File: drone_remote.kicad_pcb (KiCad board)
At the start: 2 copper layers, 7 x 9.2 mm, 99 parts, among them J1 USBC, J10 HEADER_C, J2 BAT, J3 UART, J4 SWI, J5 OLDED_SMALL, J6 OLED_BIG, J7 RFM_SOCKET, J8 RFM_SOCKET, J9 HEADER_AB, Q1 PMOS, SW1 RST_BTN, SW2 PUSH_BTN_U, SW3 PUSH_BTN_L, SW4 PUSH_BTN_R, SW5 PUSH_BTN_D, SW6 ENC1, SW7 ENC2, U1 STM32F411RETx, U2 TC1262-33, U3 SN74ALVC14PWR, U4 SN74ALVC14PWR, U5 INA180A2, U6 FT230XS, X1 32.768KHz, X2 8MHz

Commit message: update
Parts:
- removed C11: 12p, Capacitor_SMD:C_0402_1005Metric
- removed C12: 36p, Capacitor_SMD:C_0402_1005Metric
- removed C18: 100n, Capacitor_SMD:C_0805_2012Metric
- removed D7: UART_TX, LED_SMD:LED_0201_0603Metric
- removed D8: HEARTBEAT, Inductor_SMD:L_0201_0603Metric
- removed J10: HEADER_C, Connector_PinSocket_1.27mm:PinSocket_2x16_P1.27mm_Vertical
- removed J9: HEADER_AB, Connector_PinSocket_1.27mm:PinSocket_2x16_P1.27mm_Vertical
- removed JP2: BLK_OFF, Connector_PinSocket_1.27mm:PinSocket_1x02_P1.27mm_Vertical
- removed JP3: BLK_ON, Connector_PinSocket_1.27mm:PinSocket_1x02_P1.27mm_Vertical
- removed R14, R15: 660, Resistor_SMD:R_0805_2012Metric
- removed R9: 0.1, Resistor_SMD:R_0805_2012Metric
- removed U5: INA180A2, Package_TO_SOT_SMD:SOT-23-5
- removed X2: 8MHz, CRYSTAL_ECS-80-18-5PX-TR_ECS:CRYSTAL_ECS-80-18-5PX-TR_ECS
- added C33: 100n, Capacitor_SMD:C_0805_2012Metric, F.Cu at (164.2, 116.8)
- added H1: MountingHole, MountingHole:MountingHole_2.2mm_M2, F.Cu at (114.0, 76.5)
- added H2: MountingHole, MountingHole:MountingHole_2.2mm_M2, F.Cu at (114.0, 149.1)
- added H3: MountingHole, MountingHole:MountingHole_2.2mm_M2, F.Cu at (258.5, 76.5)
- added H4: MountingHole, MountingHole:MountingHole_2.2mm_M2, F.Cu at (258.5, 149.0)
- added JP1: Jumper_2_Bridged, Connector_PinHeader_2.54mm:PinHeader_1x02_P2.54mm_Vertical, F.Cu at (120.6, 81.8)
- added JP4: Jumper_2_Bridged, Connector_PinHeader_2.54mm:PinHeader_1x02_P2.54mm_Vertical, F.Cu at (147.0, 115.6)
- C10: value 12p -> 1u
- C13: value 36p -> 10p
- C14: value 100n -> 10p; footprint Capacitor_SMD:C_0805_2012Metric -> Capacitor_SMD:C_0402_1005Metric
- C15: value 1u -> 100n
- C17: value 0.1u -> 1u
- C19: value 47p -> 100n; footprint Capacitor_SMD:C_0201_0603Metric -> Capacitor_SMD:C_0805_2012Metric
- C2, C3, C4, C5, C6, C7, C8, C9: footprint Capacitor_SMD:C_0805_2012Metric -> Capacitor_SMD:C_0402_1005Metric
- C21: value 100n -> 47p; footprint Capacitor_SMD:C_0805_2012Metric -> Capacitor_SMD:C_0201_0603Metric
- D1, D2, D3: footprint Diode_SMD:D_0201_0603Metric -> Diode_SMD:D_0402_1005Metric
- D6: value UART_RX -> HEARTBEAT; footprint LED_SMD:LED_0201_0603Metric -> Inductor_SMD:L_0201_0603Metric
- J1: footprint SAMESKY_UJ20-C-H-G-MSMT-3-P16-TR:SAMESKY_UJ20-C-H-G-MSMT-3-P16-TR -> drone_remote:GCT_USB4105-GF-A
- J2: value BAT -> Conn_01x02_Socket; footprint Connector_PinSocket_2.54mm:PinSocket_1x02_P2.54mm_Vertical -> Connector_PinHeader_2.54mm:PinHeader_1x02_P2.54mm_Vertical
- J4: value SWI -> Conn_01x05_Pin; footprint Connector_PinSocket_1.00mm:PinSocket_1x05_P1.00mm_Vertical -> Connector_PinHeader_2.54mm:PinHeader_1x05_P2.54mm_Vertical
- J5: value OLDED_SMALL -> Conn_01x04_Socket; footprint Connector_PinSocket_1.00mm:PinSocket_1x04_P1.00mm_Vertical -> Connector_PinSocket_2.54mm:PinSocket_1x04_P2.54mm_Vertical
- J6: value OLED_BIG -> Conn_01x08_Socket; footprint Connector_PinSocket_1.00mm:PinSocket_1x08_P1.00mm_Vertical -> Connector_PinSocket_2.54mm:PinSocket_1x08_P2.54mm_Vertical
- J7, J8: value RFM_SOCKET -> Conn_01x09_Socket; footprint Connector_PinSocket_1.00mm:PinSocket_1x09_P1.00mm_Vertical -> Connector_PinSocket_2.54mm:PinSocket_1x09_P2.54mm_Vertical
- L1: value L_VDDA -> 120R; footprint Inductor_SMD:L_0805_2012Metric -> Inductor_SMD:L_0603_1608Metric
- L2: value L_UART -> 120R; footprint Inductor_SMD:L_0805_2012Metric -> Inductor_SMD:L_0603_1608Metric
- R1: value 47k -> 10k
- R2: value 2k -> 660
- R5: value 660 -> 10k
- SW2: value PUSH_BTN_U -> RST_BTN
- SW3: value PUSH_BTN_L -> RST_BTN
- SW4: value PUSH_BTN_R -> RST_BTN
- SW5: value PUSH_BTN_D -> RST_BTN
- X1: value 32.768KHz -> 8MHZ; footprint XTAL_7X-TR_ECS:XTAL_7X-TR_ECS -> ECS-80-10:SMD_ECS-80-10-3M-TR_ECS
- moved J3 185.2 mm to (212.3, 81.2), turned to 180 degrees
- moved C14 182.4 mm to (186.5, 120.4), turned to 180 degrees
- moved L2 179.7 mm to (215.7, 90.2), turned to -90 degrees
- moved C19 179.5 mm to (216.7, 87.3), turned to 180 degrees
- moved C20 175.5 mm to (211.9, 84.8), turned to 0 degrees
- moved J1 174.4 mm to (186.2, 75.9), turned to 180 degrees
- moved R13 170.6 mm to (212.1, 88.7), turned to 90 degrees
- moved R12 168.7 mm to (209.8, 88.7), turned to -90 degrees
- moved D1 167.1 mm to (187.3, 82.8), turned to 0 degrees
- moved D2 165.6 mm to (185.1, 82.8), turned to 180 degrees
- moved J2 164.7 mm to (173.5, 77.1), turned to -90 degrees
- moved R7 162.6 mm to (193.9, 78.0), turned to 0 degrees
- moved C21 161.2 mm to (210.2, 84.8), turned to 180 degrees
- moved D3 153.9 mm to (176.6, 82.0)
- moved U6 153.6 mm to (210.8, 94.7), turned to 180 degrees
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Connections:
- net Net-(D4-A) renamed /V_USB
- net Net-(D5-A) renamed /V_BAT
- net Net-(J2-Pin_2) renamed +5V
- net Net-(U6-USBDM) renamed /USBD-
- net Net-(U6-USBDP) renamed /USBD+
- net RFM_nRST renamed /RFM_nRST
- net SPI1_MISO renamed /SPI1_MISO
- net SPI1_MOSI renamed /SPI1_MOSI
- net SPI1_SCK renamed /SPI1_SCK
- net SPI1_nCS renamed /SPI1_nCS
- net SWCLK renamed /SWCLK
- C10 pad 1: GND -> +3.3V
- C10 pad 2: Net-(U1-PC15) -> GND
- C13 pad 2: Net-(U1-PH1) -> /OSC_OUT
- C14 pad 2: Net-(D3-A1) -> /OSC_IN
- C15 pad 1: Net-(D4-K) -> GND
- C15 pad 2: GND -> VBUS
- C16 pad 1: 3.3V -> /REG_IN
- C17 pad 1: 3.3V -> +3.3V
- C19 pad 1: Net-(J3-D-) -> GND
- C19 pad 2: GND -> Net-(J3-VBUS)
- C2 pad 1: 3.3V -> GND
- C2 pad 2: GND -> +3.3V
- C20 pad 1: Net-(J3-D+) -> /D-
- C21 pad 1: Net-(U6-3V3OUT) -> /D+
- C22 pad 1: GND -> Net-(U6-3V3OUT)
- C22 pad 2: Net-(U3-1A) -> GND
- C23 pad 2: Net-(U3-2A) -> /SW2
- C24 pad 1: Net-(U3-4A) -> GND
- C24 pad 2: GND -> /SW3
- C25 pad 2: Net-(U3-3A) -> /SW4
- C26 pad 1: GND -> /SW5
- C26 pad 2: Net-(U4-1A) -> GND
- C27 pad 1: Net-(U4-2A) -> GND
- C27 pad 2: GND -> /ENC1_A
- C28 pad 1: Net-(U4-3A) -> /ENC1_C
- C29 pad 1: GND -> /ENC1_SW
- C29 pad 2: Net-(U4-6A) -> GND
- C3 pad 2: 3.3V -> +3.3V
- C30 pad 2: Net-(U4-5A) -> /ENC2_A
- C31 pad 2: Net-(U4-4A) -> /ENC2_C
- C32 pad 2: nRST -> /ENC2_SW
- C4 pad 2: 3.3V -> +3.3V
- C5 pad 2: 3.3V -> +3.3V
- C6 pad 2: 3.3V -> +3.3V
- C7 pad 2: 3.3V -> +3.3V
- C8 pad 2: 3.3V -> +3.3VA
- C9 pad 1: GND -> +3.3VA
- C9 pad 2: 3.3V -> GND
- D1 pad 1: USB_OTG_FS_DM -> /USB_OTG_FS-
- D2 pad 1: USB_OTG_FS_DP -> /USB_OTG_FS+
- D3 pad 1: Net-(D3-A1) -> VBUS
- D4 pad 1: Net-(D4-K) -> /REG_IN
- D5 pad 1: Net-(D4-K) -> /REG_IN
- D6 pad 1: Net-(D6-K) -> GND
- F1 pad 1: Net-(D3-A1) -> VBUS
- J1 pad A4_B9: Net-(D3-A1) -> VBUS
- J1 pad A6: USB_OTG_FS_DP -> unconnected-(J1-DP1-PadA6)
- J1 pad A7: USB_OTG_FS_DM -> unconnected-(J1-DN1-PadA7)
- J1 pad B6: unconnected-(J1-DP2-PadB6) -> /USB_OTG_FS+
- J1 pad B7: unconnected-(J1-DN2-PadB7) -> /USB_OTG_FS-
- J3 pad 2: Net-(J3-D-) -> /D-
- J3 pad 3: Net-(J3-D+) -> /D+
- J3 pad 6: GND -> unconnected-(J3-Shield-Pad6)
- J4 pad 1: GND -> +3.3V
- J4 pad 2: nRST -> /SWDIO
- J4 pad 4: SWDIO -> /nRST
- J4 pad 5: 3.3V -> GND
- J5 pad 1: 3.3V -> /I2C1_SDA
- J5 pad 2: GND -> /I2C1_SCL
- J5 pad 3: I2C1_SCL -> GND
- J5 pad 4: I2C1_SDA -> +3.3V
- J6 pad 2: 3.3V -> +3.3V
- J6 pad 3: SPI2_SCK -> /SPI3_SCK
- J6 pad 4: SPI2_MOSI -> /SPI3_MOSI
- J6 pad 5: ST7735_nRESET -> /ST7735_nRST
- J6 pad 6: ST7735_DC -> /ST7735_DC
- J6 pad 7: SPI2_NSS -> /SPI3_nCS
- J7 pad 1: 3.3V -> +3.3V
- J7 pad 3: RFM_EN -> /RFM_EN
- J7 pad 9: RFM__G0 -> /RFM_G0
- L1 pad 1: 3.3V -> +3.3VA
- L1 pad 2: Net-(U1-VDDA) -> +3.3V
- R1 pad 1: Net-(U1-BOOT0) -> GND
- R1 pad 2: GND -> /BOOT0
- R10 pad 1: Net-(D4-K) -> /REG_IN
- R10 pad 2: ADC_VOLTAGE -> /ADC_VOLTAGE
- R11 pad 1: ADC_VOLTAGE -> /ADC_VOLTAGE
- R12 pad 1: Net-(J3-D+) -> /D+
- R13 pad 2: Net-(J3-D-) -> /D-
- R16 pad 1: Net-(U3-1A) -> /SW2
- R16 pad 2: 3.3V -> +3.3V
- R17 pad 1: Net-(U3-2A) -> /SW3
- R17 pad 2: 3.3V -> +3.3V
- R18 pad 1: 3.3V -> +3.3V
- R18 pad 2: Net-(U3-4A) -> /SW5
- R19 pad 1: Net-(U3-3A) -> /SW4
- R19 pad 2: 3.3V -> +3.3V
- R2 pad 1: 3.3V -> Net-(D6-A)
- R2 pad 2: Net-(U1-BOOT0) -> /HB_LED
- R20 pad 1: Net-(U4-1A) -> /ENC1_A
- R20 pad 2: 3.3V -> +3.3V
- R21 pad 1: 3.3V -> +3.3V
- R21 pad 2: Net-(U4-2A) -> /ENC1_C
- R22 pad 1: 3.3V -> +3.3V
- R22 pad 2: Net-(U4-3A) -> /ENC1_SW
- R23 pad 1: Net-(U4-6A) -> /ENC2_A
- R23 pad 2: 3.3V -> +3.3V
- R24 pad 1: Net-(U4-5A) -> /ENC2_C
- R24 pad 2: 3.3V -> +3.3V
- R25 pad 1: Net-(U4-4A) -> /ENC2_SW
- R25 pad 2: 3.3V -> +3.3V
- R26 pad 2: 3.3V -> +3.3V
- R3 pad 1: SWDIO -> /SWDIO
- R3 pad 2: 3.3V -> +3.3V
- R4 pad 2: 3.3V -> +3.3V
- R5 pad 1: Net-(D8-A) -> Net-(J6-Pin_8)
- R5 pad 2: PC13 -> GND
- R6 pad 2: PC10 -> /MCU_LED
- SW1 pad 1: nRST -> /nRST
- SW1 pad 3: nRST -> /nRST
- SW2 pad 2: GND -> /SW2
- SW2 pad 3: Net-(U3-1A) -> GND
- SW2 pad 4: Net-(U3-1A) -> /SW2
- SW3 pad 2: GND -> /SW3
- SW3 pad 3: Net-(U3-2A) -> GND
- SW3 pad 4: Net-(U3-2A) -> /SW3
- SW4 pad 2: GND -> /SW4
- SW4 pad 3: Net-(U3-3A) -> GND
- SW4 pad 4: Net-(U3-3A) -> /SW4
- SW5 pad 2: GND -> /SW5
- SW5 pad 3: Net-(U3-4A) -> GND
- SW5 pad 4: Net-(U3-4A) -> /SW5
- SW6 pad A: Net-(U4-2A) -> /ENC1_C
- SW6 pad B: Net-(U4-1A) -> /ENC1_A
- SW6 pad S1: Net-(U4-3A) -> /ENC1_SW
- SW7 pad A: Net-(U4-6A) -> /ENC2_C
- SW7 pad B: Net-(U4-5A) -> /ENC2_A
- SW7 pad C: unconnected-(SW7-PadC) -> GND
- SW7 pad S1: GND -> /ENC2_SW
- SW7 pad S2: Net-(U4-4A) -> GND
- U1 pad 1: 3.3V -> +3.3V
- U1 pad 10: RFM__G0 -> unconnected-(U1-PC2-Pad10)
- U1 pad 11: PUSH_BTN3 -> unconnected-(U1-PC3-Pad11)
- U1 pad 13: Net-(U1-VDDA) -> +3.3VA
- U1 pad 14: TIM2_CH1 -> /TIM2_CH1
- U1 pad 15: TIM2_CH2 -> /TIM2_CH2
- U1 pad 16: ST7735_DC -> /ENC2_BTN
- U1 pad 17: ST7735_nRESET -> /ENC1_BTN
- U1 pad 19: 3.3V -> +3.3V
- U1 pad 2: PC13 -> /PUSH_BTN2
- U1 pad 24: PUSH_BTN4 -> /RFM_EN
- U1 pad 26: RFM_EN -> /RFM_G0
- U1 pad 27: PUSH_BTN1 -> /ADC_VOLTAGE
- U1 pad 28: PUSH_BTN2 -> /MCU_LED
- U1 pad 29: SPI2_SCK -> /HB_LED
- U1 pad 3: Net-(U1-PC14) -> /PUSH_BTN3
- U1 pad 32: 3.3V -> +3.3V
- U1 pad 33: SPI2_NSS -> unconnected-(U1-PB12-Pad33)
- U1 pad 34: ENC2_BTN -> unconnected-(U1-PB13-Pad34)
- U1 pad 35: ENC1_BTN -> unconnected-(U1-PB14-Pad35)
- U1 pad 36: SPI2_MOSI -> unconnected-(U1-PB15-Pad36)
- U1 pad 37: USART_TX -> unconnected-(U1-PC6-Pad37)
- U1 pad 38: USART_RX -> unconnected-(U1-PC7-Pad38)
- U1 pad 39: PC8 -> unconnected-(U1-PC8-Pad39)
- U1 pad 4: Net-(U1-PC15) -> /PUSH_BTN4
- U1 pad 40: PC9 -> unconnected-(U1-PC9-Pad40)
- U1 pad 41: PA8 -> unconnected-(U1-PA8-Pad41)
- U1 pad 42: PA9 -> /USART_TX
- U1 pad 43: PA10 -> /USART_RX
- U1 pad 44: USB_OTG_FS_DP -> /USB_OTG_FS-
- U1 pad 45: USB_OTG_FS_DM -> /USB_OTG_FS+
- U1 pad 46: SWDIO -> /SWDIO
- U1 pad 48: 3.3V -> +3.3V
- U1 pad 5: Net-(U1-PH0) -> /OSC_IN
- U1 pad 50: PA15 -> /SPI3_nCS
- U1 pad 51: PC10 -> /SPI3_SCK
- U1 pad 52: PC11 -> unconnected-(U1-PC11-Pad52)
- U1 pad 53: PC12 -> /SPI3_MOSI
- U1 pad 54: PD2 -> /ST7735_nRST
- U1 pad 55: PB3 -> unconnected-(U1-PB3-Pad55)
- U1 pad 56: TIM3_CH1 -> /ST7735_DC
- U1 pad 57: TIM3_CH2 -> /PUSH_BTN1
- U1 pad 58: I2C1_SCL -> /TIM4_CH1
- U1 pad 59: I2C1_SDA -> /TIM4_CH2
- U1 pad 6: Net-(U1-PH1) -> /OSC_OUT
- U1 pad 60: Net-(U1-BOOT0) -> /BOOT0
- U1 pad 61: PB8 -> /I2C1_SCL
- U1 pad 62: PB9 -> /I2C1_SDA
- U1 pad 64: 3.3V -> +3.3V
- U1 pad 7: nRST -> /nRST
- U1 pad 8: ADC_CURRENT_SENSE -> unconnected-(U1-PC0-Pad8)
- U1 pad 9: ADC_VOLTAGE -> unconnected-(U1-PC1-Pad9)
- U2 pad 1: Net-(D4-K) -> /REG_IN
- U2 pad 3: 3.3V -> +3.3V
- U3 pad 1: Net-(U3-1A) -> /SW2
- U3 pad 12: unconnected-(U3-6Y-Pad12) -> /PUSH_BTN4
- U3 pad 13: unconnected-(U3-6A-Pad13) -> /SW5
- U3 pad 14: 3.3V -> +3.3V
- U3 pad 2: PUSH_BTN1 -> /PUSH_BTN1
- U3 pad 3: Net-(U3-2A) -> /SW3
- U3 pad 4: PUSH_BTN2 -> /PUSH_BTN2
- U3 pad 5: Net-(U3-3A) -> /SW4
- U3 pad 6: PUSH_BTN3 -> /PUSH_BTN3
- U3 pad 8: PUSH_BTN4 -> unconnected-(U3-4Y-Pad8)
- U3 pad 9: Net-(U3-4A) -> unconnected-(U3-4A-Pad9)
- U4 pad 1: Net-(U4-1A) -> /ENC1_A
- U4 pad 10: TIM3_CH2 -> /TIM2_CH2
- U4 pad 11: Net-(U4-5A) -> /ENC2_C
- U4 pad 12: TIM3_CH1 -> /TIM2_CH1
- U4 pad 13: Net-(U4-6A) -> /ENC2_A
- U4 pad 14: 3.3V -> +3.3V
- U4 pad 2: TIM2_CH1 -> /TIM4_CH1
- U4 pad 3: Net-(U4-2A) -> /ENC1_C
- U4 pad 4: TIM2_CH2 -> /TIM4_CH2
- U4 pad 5: Net-(U4-3A) -> /ENC1_SW
- U4 pad 6: ENC1_BTN -> /ENC1_BTN
- U4 pad 8: ENC2_BTN -> /ENC2_BTN
- U4 pad 9: Net-(U4-4A) -> /ENC2_SW
- U6 pad 1: USART_TX -> /USART_TX
- U6 pad 14: Net-(D6-K) -> unconnected-(U6-CBUS1-Pad14)
- U6 pad 4: USART_RX -> /USART_RX
- U6 pad 7: Net-(D7-K) -> unconnected-(U6-CBUS2-Pad7)
- X1 pad 1: Net-(U1-PC15) -> /OSC_IN
- X1 pad 2: Net-(U1-PC14) -> GND
- X1 pad 3: (no net) -> /OSC_OUT
- X1 pad 4: (no net) -> GND
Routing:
- net +3.3V: track 0.00 -> 620.3 mm, vias 0 -> 27
- net GND: track 66.9 -> 210.1 mm, vias 2 -> 35
- net 3.3V: track 70.4 -> 0.00 mm
- net /I2C1_SDA: track 0.00 -> 68.4 mm
- net /SPI3_nCS: track 0.00 -> 67.2 mm
- net /ENC1_SW: track 0.00 -> 66.8 mm
- net /I2C1_SCL: track 0.00 -> 65.6 mm
- net /ST7735_DC: track 0.00 -> 64.9 mm
- net /ST7735_nRST: track 0.00 -> 62.0 mm
- net /RFM_G0: track 0.00 -> 59.8 mm
- net /SPI3_MOSI: track 0.00 -> 59.2 mm
- net Net-(U3-3A): track 59.0 -> 0.00 mm
- net /SPI3_SCK: track 0.00 -> 56.3 mm
- net /SW4: track 0.00 -> 53.6 mm
- net /nRST: track 0.00 -> 52.3 mm
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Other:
- board size 7 x 9.2 mm -> 151 x 78.8 mm

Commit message: updates
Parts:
- removed the J1 at (186.2, 75.9)
- added J3: GSB1C411101DS1HR, pcb_project:AMPHENOL_GSB1C411101DS1HR, F.Cu at (92.0, 35.1)
- C1: renamed from C20; footprint Capacitor_SMD:C_0201_0603Metric -> Capacitor_SMD:C_0402_1005Metric
- C2: renamed from C21; footprint Capacitor_SMD:C_0201_0603Metric -> Capacitor_SMD:C_0402_1005Metric
- D6: footprint Inductor_SMD:L_0201_0603Metric -> LED_SMD:LED_0603_1608Metric
- D7: renamed from D10; footprint Resistor_SMD:R_0201_0603Metric -> LED_SMD:LED_0603_1608Metric
- D8: renamed from D9; footprint LED_SMD:LED_0201_0603Metric -> LED_SMD:LED_0603_1608Metric
- H1, H2, H3, H4: footprint MountingHole:MountingHole_2.2mm_M2 -> MountingHole:MountingHole_2.7mm_M2.5
- J2: renamed from J3; footprint 690-005-299-043_EDA:690-005-299-043_EDA -> pcb_project:CONN5_USB1734035_NP_TEC
- SW1, SW4, SW5: footprint SW4_1825910-B_TEC:SW4_1825910-B_TEC -> pcb_project:SW_1825910-6-4
- SW2: renamed from SW3; footprint SW4_1825910-B_TEC:SW4_1825910-B_TEC -> pcb_project:SW_1825910-6-4
- SW3: renamed from SW2; footprint SW4_1825910-B_TEC:SW4_1825910-B_TEC -> pcb_project:SW_1825910-6-4
- SW6, SW7: footprint Rotary_Encoder:RotaryEncoder_Alps_EC11E-Switch_Vertical_H20mm -> Rotary_Encoder:RotaryEncoder_Bourns_Vertical_PEC12R-3x17F-Sxxxx
- U4: renamed from U3; footprint SN74ALVC14PWR:PW14 -> Package_SO:SSOP-14_5.3x6.2mm_P0.65mm
- U5: renamed from U4; footprint SN74ALVC14PWR:PW14 -> Package_SO:SSOP-14_5.3x6.2mm_P0.65mm
- X1: footprint ECS-80-10:SMD_ECS-80-10-3M-TR_ECS -> pcb_project:XTAL_ECS-80-10-30B-CWN-TR
- moved L1 126.2 mm to (96.3, 49.3)
- moved C3 125.3 mm to (101.5, 38.1), turned to -90 degrees
- moved U4 123.9 mm to (58.5, 75.7)
- moved R5 121.6 mm to (39.4, 67.9)
- moved H3 121.0 mm to (144.1, 37.0)
- moved R13 120.0 mm to (48.7, 84.9), turned to 180 degrees
- moved JP1 119.8 mm to (36.0, 70.5)
- moved H4 119.7 mm to (144.0, 114.0)
- moved R4 117.3 mm to (84.5, 35.6), turned to 90 degrees
- moved J1 117.1 mm to (69.3, 54.6), turned to 90 degrees
- moved D8 116.8 mm to (112.0, 54.9)
- moved R11 116.4 mm to (84.2, 44.6)
- moved C5 115.3 mm to (98.6, 49.5), turned to 90 degrees
- moved U1 115.2 mm to (103.7, 52.4)
- moved R3 115.0 mm to (104.6, 47.8)
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- renumbered C3 to C10, C2 to C11, C8 to C12, C9 to C13, C10 to C14, C1 to C15, C14 to C16, C13 to C17, C15 to C18, C16 to C19, C17 to C20, C24 to C21, C25 to C22, C26 to C24, C27 to C25, C28 to C26, C29 to C27, C31 to C28, C32 to C29, C19 to C3, C33 to C4, C22 to C5, C7 to C6, C6 to C7, C5 to C8, C4 to C9, D5 to D4, D4 to D5, J4 to J1, J2 to J4, J6 to J5, J5 to J6, JP4 to JP1, JP1 to JP2, L2 to L1, L1 to L2, R8 to R1, R17 to R10, R10 to R11, R11 to R12, R16 to R13, R19 to R14, R18 to R15, R5 to R16, R26 to R17, R20 to R18, R21 to R19, R12 to R2, R22 to R20, R23 to R21, R24 to R22, R25 to R23, R13 to R3, R7 to R4, R1 to R5, R2 to R6, R6 to R7, R3 to R8, R4 to R9, U6 to U1, U1 to U2, U2 to U3
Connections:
- R1 pad 1: Net-(J1-CC2) -> GND
- R1 pad 2: GND -> Net-(J3-CC1)
- R8 pad 1: /SWDIO -> +3.3V
- R8 pad 2: +3.3V -> /SWDIO
- R9 pad 1: /SWCLK -> +3.3V
- R9 pad 2: +3.3V -> /SWCLK
- U4 pad 1: /SW2 -> /SW4
- U4 pad 3: /SW3 -> /SW2
- U4 pad 5: /SW4 -> /SW3
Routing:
- net /MCU_LED: track 13.9 -> 48.3 mm
- net /HB_LED: track 10.7 -> 45.1 mm
- net /TIM4_CH1: track 11.0 -> 37.6 mm, vias 0 -> 2
- net /ST7735_DC: track 64.9 -> 42.1 mm
- net /I2C1_SCL: track 65.6 -> 43.3 mm
- net /I2C1_SDA: track 68.4 -> 46.0 mm
- net /ST7735_nRST: track 62.0 -> 39.9 mm
- net /SPI3_MOSI: track 59.2 -> 38.1 mm
- net /SWCLK: track 32.4 -> 11.3 mm
- net /SPI3_SCK: track 56.3 -> 36.2 mm
- net /REG_IN: track 38.1 -> 18.3 mm, vias 2 -> 0
- net GND: track 210.1 -> 228.2 mm, vias 35 -> 29
- net /SW4: track 53.6 -> 36.2 mm
- net /SPI1_SCK: track 40.7 -> 23.6 mm
- net /SPI3_nCS: track 67.2 -> 51.1 mm
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- added copper zone on B.Cu, net GND
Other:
- board size 151 x 78.8 mm -> 115.1 x 85.1 mm

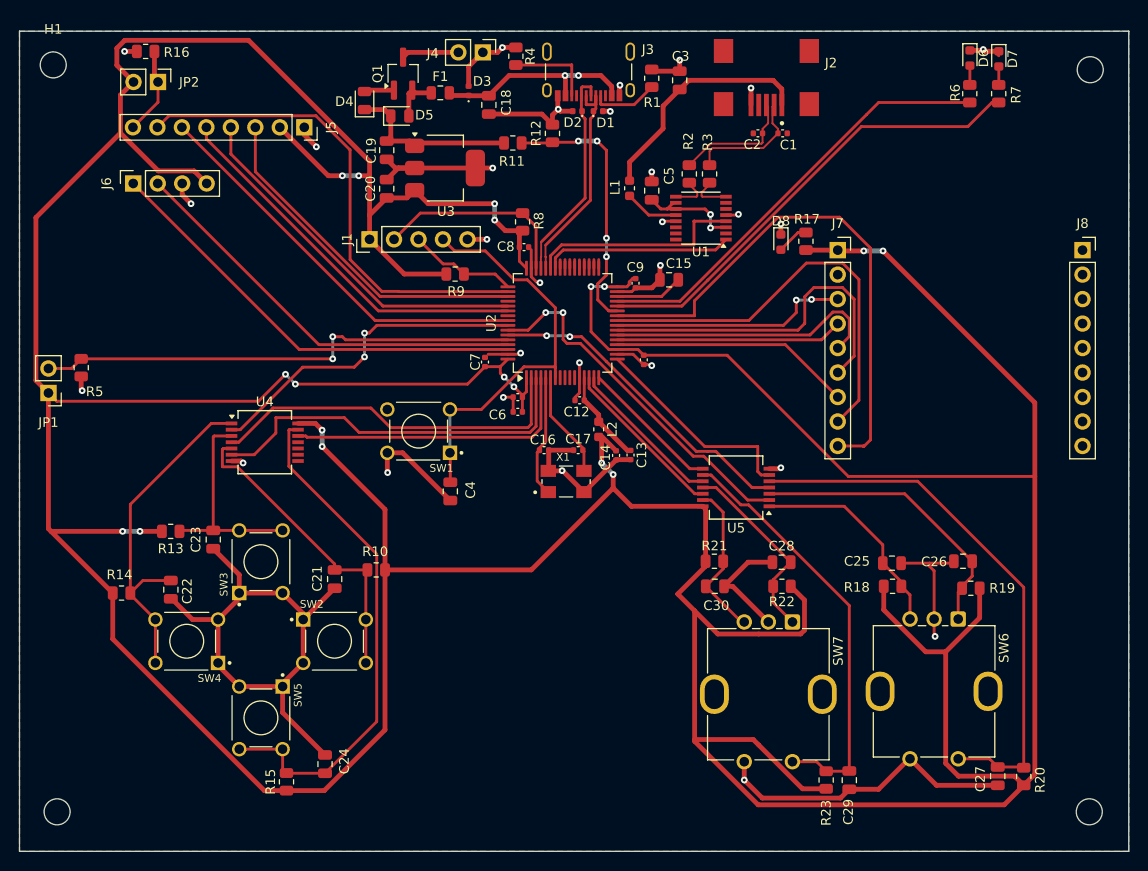
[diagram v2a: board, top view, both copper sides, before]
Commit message: finalised first version of pcb, generated manufacturing files, cleaned up file dir
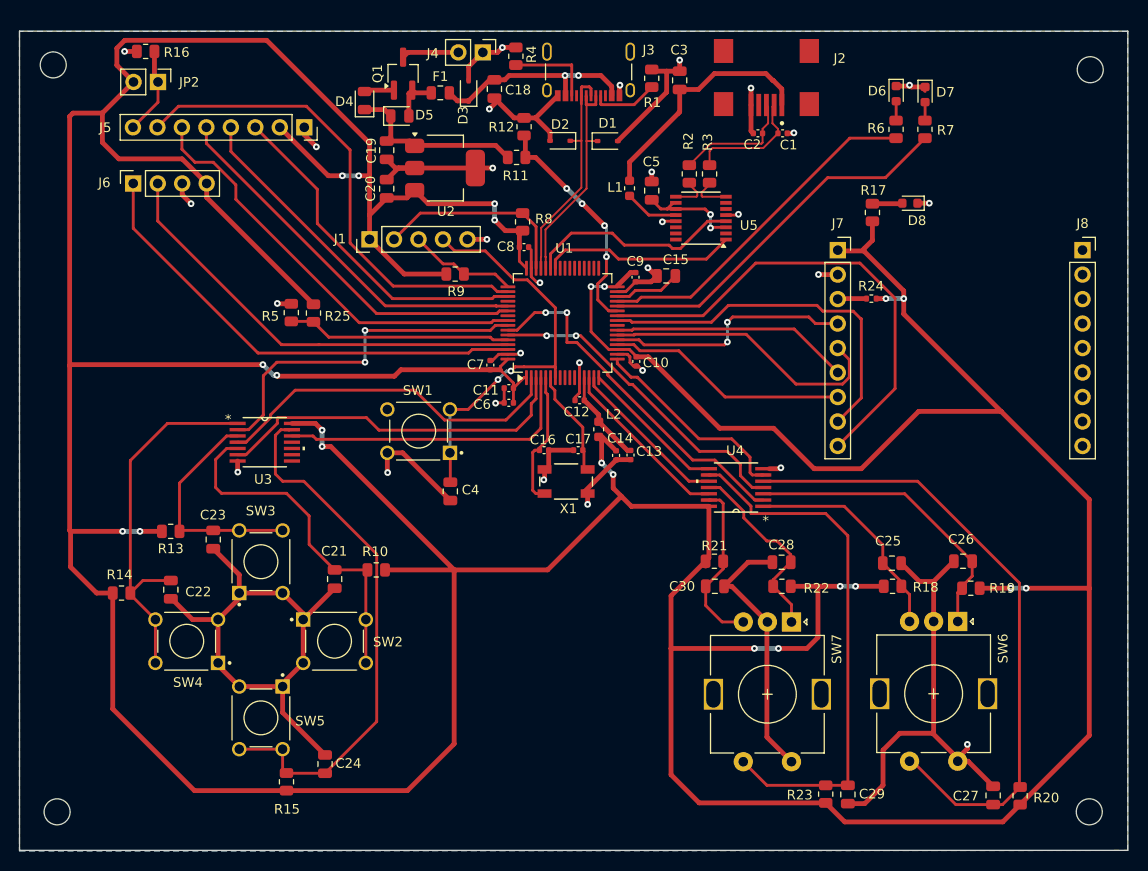
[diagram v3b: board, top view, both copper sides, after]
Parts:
- removed JP1: Jumper_2_Bridged, Connector_PinHeader_2.54mm:PinHeader_1x02_P2.54mm_Vertical
- added R24: 10k, Resistor_SMD:R_0402_1005Metric, F.Cu at (121.4, 60.8)
- added R25: 10k, Resistor_SMD:R_0805_2012Metric, F.Cu at (63.5, 62.2)
- D1, D2, D3: footprint Diode_SMD:D_0402_1005Metric -> Diode_SMD:D_SOD-323
- J2: footprint pcb_project:CONN5_USB1734035_NP_TEC -> project_library:CONN5_USB1734035_NP_TEC
- J3: footprint pcb_project:AMPHENOL_GSB1C411101DS1HR -> project_library:AMPHENOL_GSB1C411101DS1HR
- SW1, SW2, SW3, SW4, SW5: footprint pcb_project:SW_1825910-6-4 -> project_library:SW_1825910-6-4
- SW6, SW7: footprint Rotary_Encoder:RotaryEncoder_Bourns_Vertical_PEC12R-3x17F-Sxxxx -> Rotary_Encoder:RotaryEncoder_Alps_EC11E-Switch_Vertical_H20mm
- U3: renamed from U4; footprint Package_SO:SSOP-14_5.3x6.2mm_P0.65mm -> SN74ALVC14PWR:PW14
- U4: renamed from U5; footprint Package_SO:SSOP-14_5.3x6.2mm_P0.65mm -> SN74ALVC14PWR:PW14
- X1: footprint pcb_project:XTAL_ECS-80-10-30B-CWN-TR -> project_library:SMD_ECS-80-10-3M-TR_ECS
- moved R5 22.5 mm to (61.2, 62.2), turned to -90 degrees
- moved D8 14.0 mm to (125.4, 50.9), turned to 180 degrees
- moved D6 8.50 mm to (124.0, 39.5)
- moved D7 8.50 mm to (127.0, 39.6)
- moved R6 8.50 mm to (124.0, 43.2)
- moved R7 8.50 mm to (127.0, 43.2)
- moved R17 7.52 mm to (121.5, 51.8)
- moved D2 3.56 mm to (89.1, 44.4)
- moved D1 3.25 mm to (94.0, 44.4)
- moved R12 3.03 mm to (85.3, 42.9)
- moved C27 2.06 mm to (134.0, 112.3), turned to 90 degrees
- moved R20 2.03 mm to (136.8, 112.3)
- moved C18 1.75 mm to (82.3, 39.0)
- moved R11 1.55 mm to (84.6, 46.1)
- moved C29 1.50 mm to (119.0, 112.2)
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- renumbered U2 to U1, U3 to U2, U1 to U5
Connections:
- J7 pad 3: /RFM_EN -> Net-(J7-Pin_3)
- U1 pad 24: /RFM_EN -> unconnected-(U1-PC4-Pad24)
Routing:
- net GND: track 228.2 -> 257.7 mm, vias 29 -> 30
- net /BOOT0: track 50.5 -> 23.3 mm, vias 2 -> 0
- net /RFM_EN: track 24.8 -> 0.00 mm, vias 2 -> 0
- net +3.3V: track 624.8 -> 639.1 mm, vias 18 -> 22
- net /SPI1_MOSI: track 36.9 -> 24.8 mm
- net /ENC2_SW: track 44.3 -> 56.1 mm
- net /MCU_LED: track 48.3 -> 39.1 mm
- net /HB_LED: track 45.1 -> 35.9 mm
- net /ENC1_SW: track 56.9 -> 65.7 mm
- net /RFM_G0: track 56.4 -> 50.4 mm
- net /RFM_nRST: track 43.9 -> 38.4 mm
- net /SW3: track 32.3 -> 36.7 mm
- net /ADC_VOLTAGE: track 27.8 -> 24.1 mm
- net /SW5: track 53.9 -> 57.2 mm
- net /SW4: track 36.2 -> 39.5 mm
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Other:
- board size 115.1 x 85.1 mm -> 115 x 85 mm
